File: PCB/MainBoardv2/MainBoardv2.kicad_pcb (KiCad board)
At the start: 2 copper layers, 100 x 100 mm, 100 parts, among them J1 Conn_02x03_Odd_Even, J10 Conn_01x04_Socket, J11 Conn_01x03_Socket, J12 Conn_01x03_Socket, J13 Conn_01x04_Socket, J14 Conn_01x03_Socket, J15 Conn_01x03_Socket, J16 Conn_01x04_Socket, J17 Conn_01x03_Socket, J18 Conn_01x03_Socket, J19 Conn_01x04_Socket, J2 USB_B_Micro, J20 Conn_01x03_Socket, J21 Screw_Terminal_01x02, J22 Screw_Terminal_01x02, J23 Screw_Terminal_01x02, J3 Conn_02x03_Odd_Even, J4 Conn_01x05_Pin, J5 Conn_01x03_Socket, J6 Screw_Terminal_01x02, J7 Conn_01x04_Socket, J8 Screw_Terminal_01x02, J9 Conn_01x04_Socket, SW1 SW_Push, SW2 Toggle, SW3 Slide, U1 AZ1117-3.3, U2 STM32F103C8T6TR, U3 SN74HCS4075PWR, U4 TPS56637RPA, Y1 8MHz Crystal

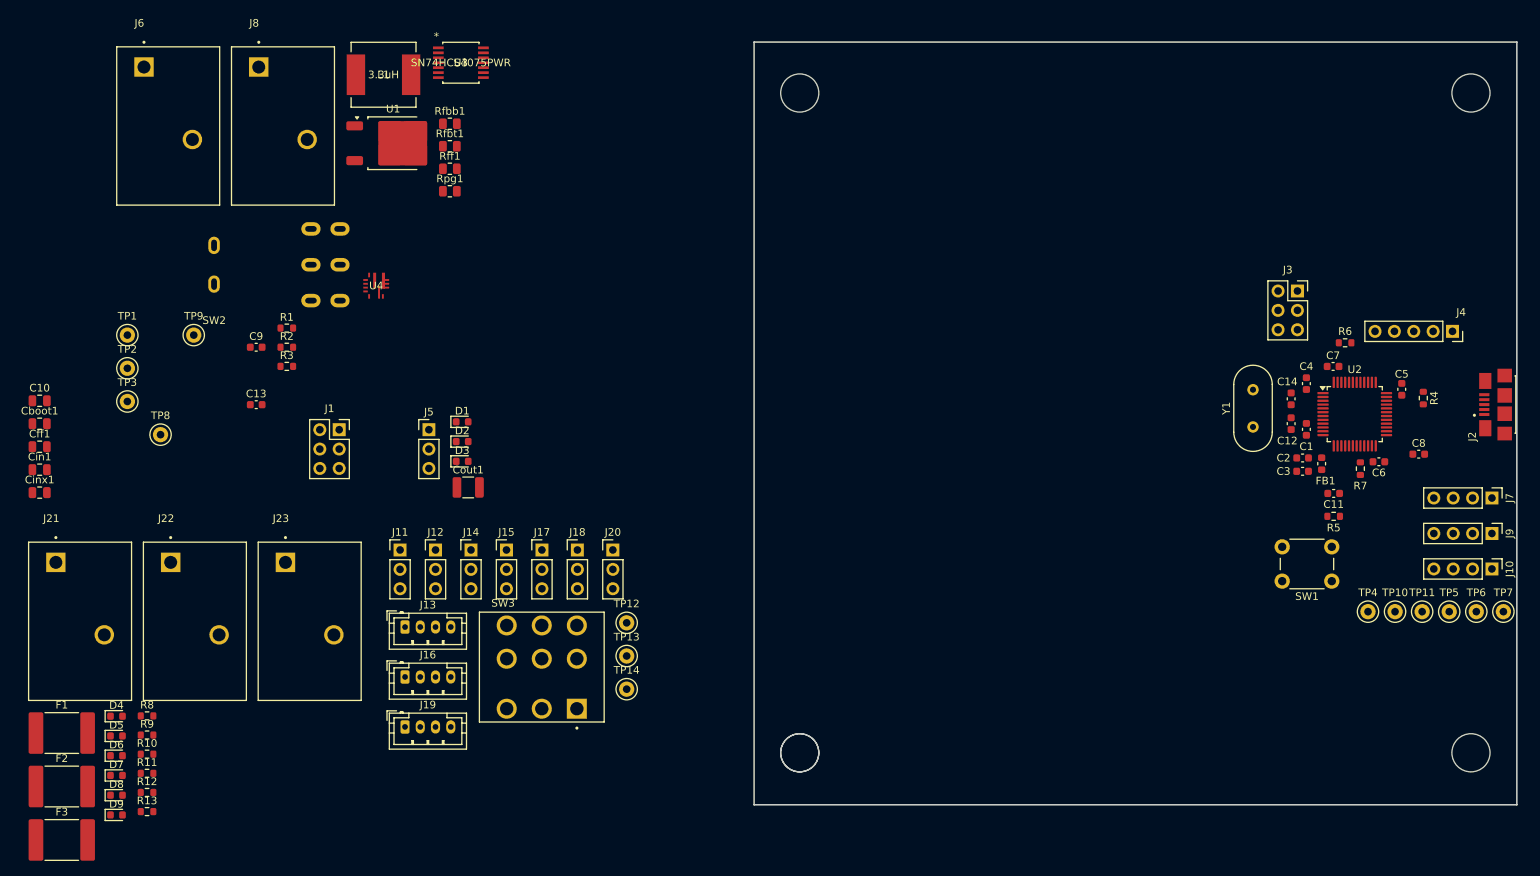
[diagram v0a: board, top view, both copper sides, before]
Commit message: Main Board v2 Rough component layout complete
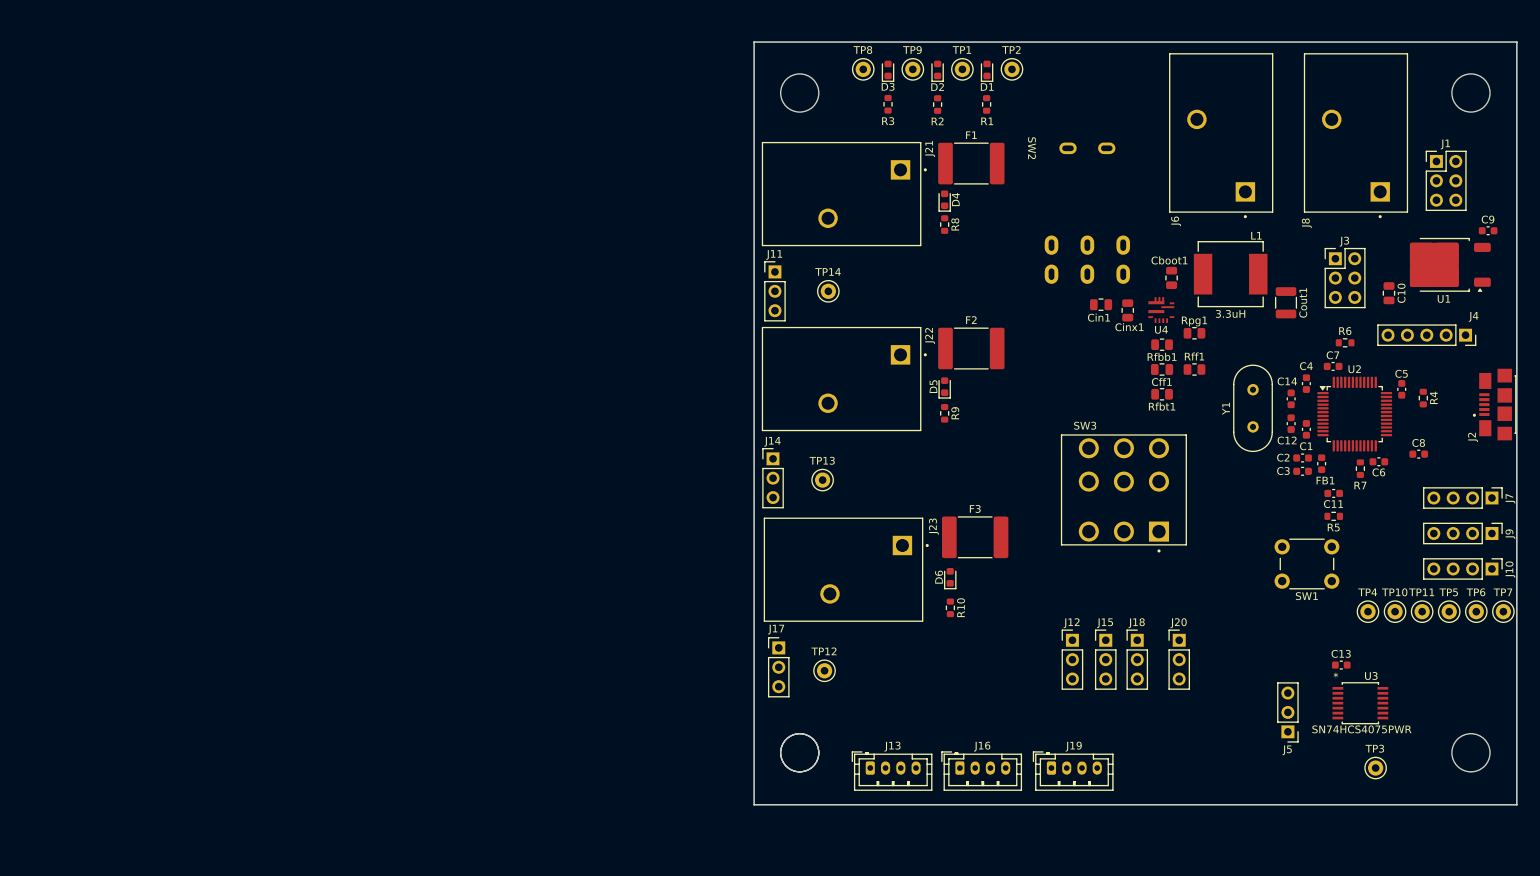
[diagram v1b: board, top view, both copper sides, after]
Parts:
- removed the D5 at (7.17, 137.5)
- removed D7, D8, D9: LED, LED_SMD:LED_0603_1608Metric
- removed R11, R13: 1.5k, Resistor_SMD:R_0603_1608Metric
- removed the R9 at (11.2, 137.4)
- added D6: LED, LED_SMD:LED_0603_1608Metric, F.Cu at (116.5, 116.8)
- J1, J3: footprint Connector_PinSocket_2.54mm:PinSocket_2x03_P2.54mm_Vertical -> Connector_PinHeader_2.54mm:PinHeader_2x03_P2.54mm_Vertical
- moved C10 177.5 mm to (174.0, 79.5), turned to -90 degrees
- moved TP3 170.6 mm to (172.2, 141.8)
- moved C9 162.2 mm to (187.0, 71.3)
- moved J8 155.4 mm to (176.4, 48.1), turned to 180 degrees
- moved J6 152.8 mm to (158.8, 48.1), turned to 180 degrees
- moved Cboot1 149.6 mm to (145.5, 77.5), turned to 90 degrees
- moved J1 148.1 mm to (180.2, 62.2)
- moved Cff1 147.5 mm to (144.2, 89.5), turned to 180 degrees
- moved C13 146.3 mm to (167.8, 128.2)
- moved U3 144.8 mm to (170.2, 133.2)
- moved Cinx1 144.6 mm to (139.8, 81.8), turned to -90 degrees
- moved Cin1 140.8 mm to (136.2, 81.0), turned to 180 degrees
- moved F1 140.7 mm to (119.2, 62.5)
- moved U1 138.7 mm to (181.2, 75.8), turned to 180 degrees
- moved F2 132.4 mm to (119.2, 86.8)
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- renumbered D6 to D5, R12 to R10, R10 to R9
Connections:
- net /PWM & Encoders/M1_PWM renamed /PWM & Encoders & Limit Switches/M1_PWM
- net /PWM & Encoders/M2_PWM renamed /PWM & Encoders & Limit Switches/M2_PWM
- net /PWM & Encoders/M3_PWM renamed /PWM & Encoders & Limit Switches/M3_PWM
- net /PWM & Encoders/RC_PWM1 renamed /PWM & Encoders & Limit Switches/RC_PWM1
- net /PWM & Encoders/RC_PWM2 renamed /PWM & Encoders & Limit Switches/RC_PWM2
- net /PWM & Encoders/RC_PWM3 renamed /PWM & Encoders & Limit Switches/RC_PWM3
- net Net-(D4-A) renamed /Motors/Motor1PowerOut
- net Net-(D6-A) renamed /Motors/Motor2PowerOut
- net Net-(D8-A) renamed /Motors/Motor3PowerOut
- net Net-(J6-Pin_2) renamed /12VPowerInput
- J1 pad 1: VBUS -> /5V_EXT
- J1 pad 5: /5V_EXT -> VBUS
- J11 pad 2: /PWM & Encoders/REG_IN -> +5V
- J14 pad 2: /PWM & Encoders/REG_IN -> +5V
- J17 pad 2: /PWM & Encoders/REG_IN -> +5V
- J20 pad 2: /PWM & Encoders/REG_IN -> +5V
- SW2 pad 3: unconnected-(SW2-C-Pad3) -> /PowerSwitchOff
- SW2 pad 6: unconnected-(SW2-C-Pad6) -> /PowerSwitchOff

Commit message: updating layout progress, adding limit switch extra circuitry
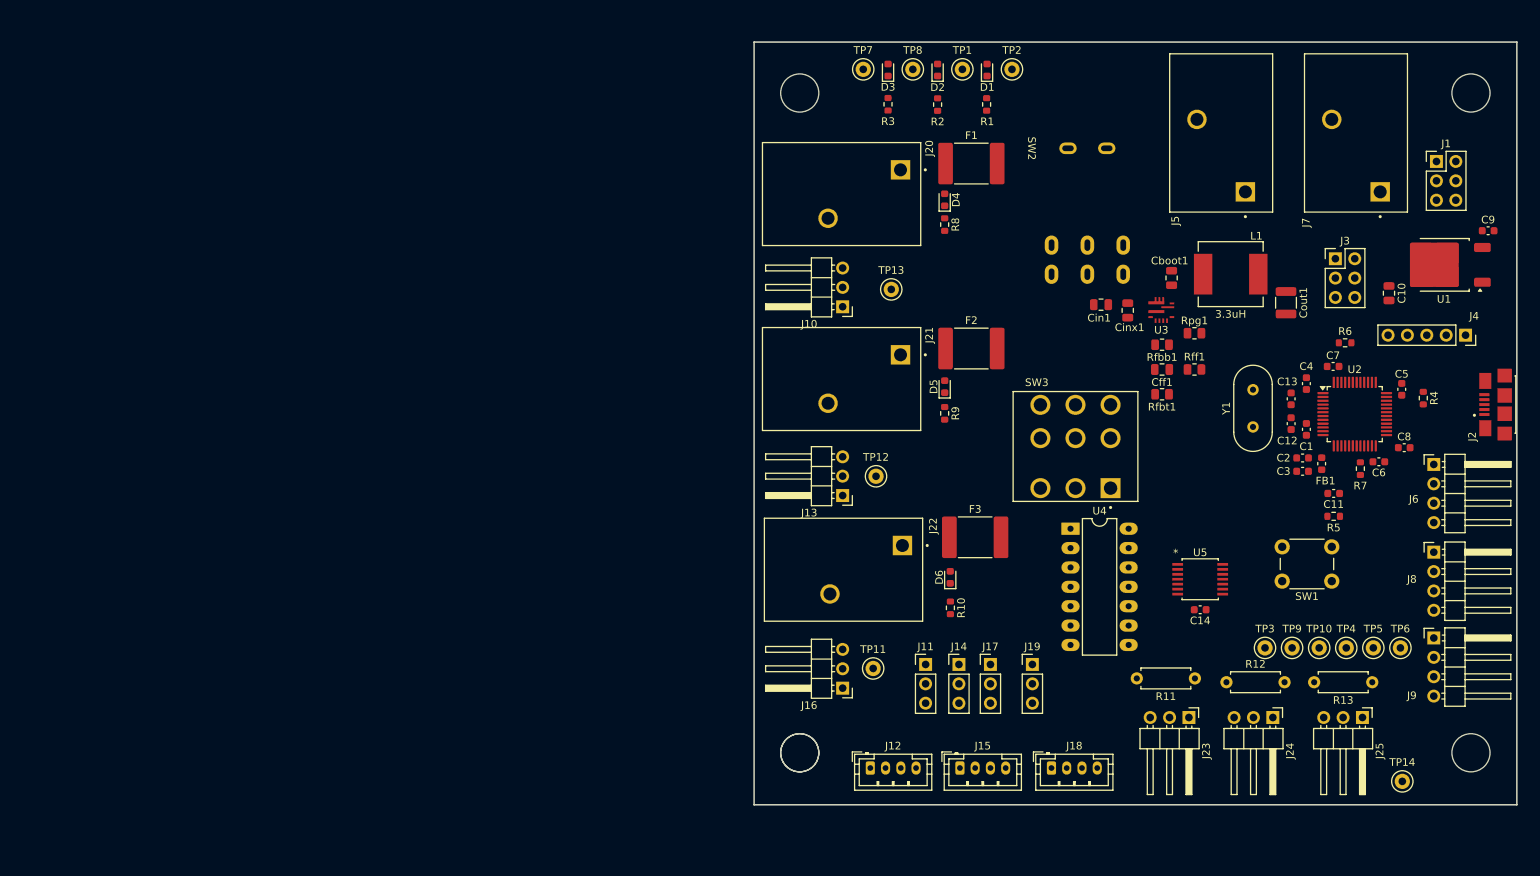
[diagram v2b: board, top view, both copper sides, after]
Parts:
- removed the C13 at (167.8, 128.2)
- removed the J5 at (160.8, 137.0)
- removed the TP3 at (172.2, 141.8)
- removed the U3 at (170.2, 133.2)
- added C14: 100n, Capacitor_SMD:C_0603_1608Metric, F.Cu at (149.2, 121.0)
- added J23: Conn_01x03_Socket, Connector_PinHeader_2.54mm:PinHeader_1x03_P2.54mm_Horizontal, F.Cu at (147.8, 135.1)
- added J24: Conn_01x03_Socket, Connector_PinHeader_2.54mm:PinHeader_1x03_P2.54mm_Horizontal, F.Cu at (158.8, 135.1)
- added J25: Conn_01x03_Socket, Connector_PinHeader_2.54mm:PinHeader_1x03_P2.54mm_Horizontal, F.Cu at (170.5, 135.1)
- added R11: 10k, Resistor_THT:R_Axial_DIN0207_L6.3mm_D2.5mm_P7.62mm_Horizontal, F.Cu at (148.6, 130.0)
- added R12: 10k, Resistor_THT:R_Axial_DIN0207_L6.3mm_D2.5mm_P7.62mm_Horizontal, F.Cu at (152.7, 130.5)
- added R13: 10k, Resistor_THT:R_Axial_DIN0207_L6.3mm_D2.5mm_P7.62mm_Horizontal, F.Cu at (171.8, 130.5)
- added TP14: White, TestPoint:TestPoint_Keystone_5000-5004_Miniature, F.Cu at (175.8, 143.5)
- added U4: CD74HC00_N_14, Package_DIP:DIP-14_W7.62mm_LongPads, F.Cu at (132.2, 110.4)
- added U5: SN74HCS4075PWR, CustomFootprints:SN74HCS4075PWR, F.Cu at (149.2, 117.0)
- J10: renamed from J11; footprint Connector_PinHeader_2.54mm:PinHeader_1x03_P2.54mm_Vertical -> Connector_PinHeader_2.54mm:PinHeader_1x03_P2.54mm_Horizontal
- J13: renamed from J14; footprint Connector_PinHeader_2.54mm:PinHeader_1x03_P2.54mm_Vertical -> Connector_PinHeader_2.54mm:PinHeader_1x03_P2.54mm_Horizontal
- J16: renamed from J17; footprint Connector_PinHeader_2.54mm:PinHeader_1x03_P2.54mm_Vertical -> Connector_PinHeader_2.54mm:PinHeader_1x03_P2.54mm_Horizontal
- J6: renamed from J7; footprint Connector_PinHeader_2.54mm:PinHeader_1x04_P2.54mm_Vertical -> Connector_PinHeader_2.54mm:PinHeader_1x04_P2.54mm_Horizontal
- J8: renamed from J9; footprint Connector_PinHeader_2.54mm:PinHeader_1x04_P2.54mm_Vertical -> Connector_PinHeader_2.54mm:PinHeader_1x04_P2.54mm_Horizontal
- J9: renamed from J10; footprint Connector_PinHeader_2.54mm:PinHeader_1x04_P2.54mm_Vertical -> Connector_PinHeader_2.54mm:PinHeader_1x04_P2.54mm_Horizontal
- moved J11 19.5 mm to (113.2, 128.2)
- moved J14 19.5 mm to (117.6, 128.2)
- moved J17 19.5 mm to (121.8, 128.2)
- moved J19 19.5 mm to (127.2, 128.2)
- moved TP10 14.3 mm to (164.8, 126.0)
- moved TP3 14.3 mm to (157.8, 126.0)
- moved TP4 14.3 mm to (168.4, 126.0)
- moved TP5 14.3 mm to (171.9, 126.0)
- moved TP6 14.3 mm to (175.5, 126.0)
- moved TP9 14.3 mm to (161.3, 126.0)
- moved J9 11.8 mm to (179.9, 124.7), turned to 0 degrees
- moved J13 10.3 mm to (102.4, 106.0), turned to 180 degrees
- moved J10 9.98 mm to (102.4, 81.3), turned to 180 degrees
- moved J16 9.90 mm to (102.4, 131.3), turned to 180 degrees
- moved J6 8.80 mm to (179.9, 102.0), turned to 0 degrees
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- renumbered C14 to C13, J12 to J11, J13 to J12, J15 to J14, J16 to J15, J18 to J17, J19 to J18, J20 to J19, J21 to J20, J22 to J21, J23 to J22, J6 to J5, J8 to J7, TP11 to TP10, TP12 to TP11, TP13 to TP12, TP14 to TP13, TP4 to TP3, TP5 to TP4, TP6 to TP5, TP7 to TP6, TP8 to TP7, TP9 to TP8, TP10 to TP9, U4 to U3

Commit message: PCB laid out & passes DRC
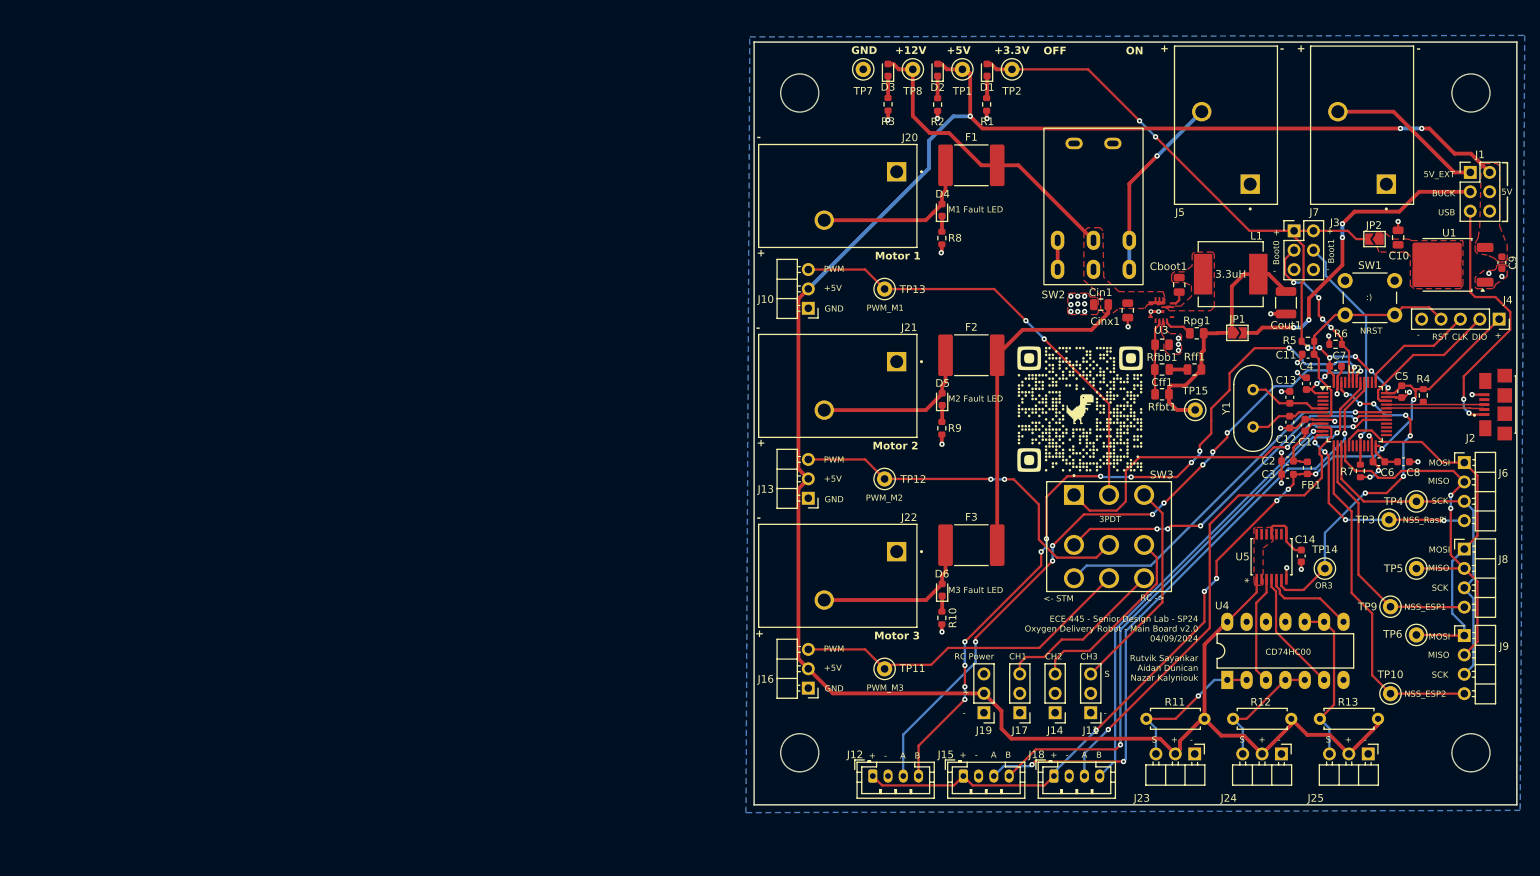
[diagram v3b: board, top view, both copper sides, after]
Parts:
- removed ?: , 
- added G***: LOGO, LOGO, F.Cu at (133.5, 94.7)
- added JP1: SolderJumper_2_Open, Jumper:SolderJumper-2_P1.3mm_Open_TrianglePad1.0x1.5mm, F.Cu at (154.1, 84.7)
- added JP2: SolderJumper_2_Open, Jumper:SolderJumper-2_P1.3mm_Open_TrianglePad1.0x1.5mm, F.Cu at (172.1, 72.4)
- added TP15: 5V_Buck, TestPoint:TestPoint_Keystone_5000-5004_Miniature, F.Cu at (148.6, 94.8)
- moved SW1 39.4 mm to (168.2, 77.8), turned to 0 degrees
- moved TP14 29.7 mm to (165.6, 115.6)
- moved U4 28.6 mm to (152.8, 130.2), turned to 90 degrees
- moved TP3 23.4 mm to (174.0, 109.2)
- moved R5 23.2 mm to (163.4, 85.8)
- moved J11 22.6 mm to (134.9, 134.5), turned to 180 degrees
- moved TP4 21.3 mm to (177.6, 106.8)
- moved C11 18.6 mm to (163.4, 87.5)
- moved C14 15.0 mm to (162.5, 113.9), turned to -90 degrees
- moved J14 14.1 mm to (130.2, 134.5), turned to 180 degrees
- moved TP9 14.0 mm to (174.2, 120.6)
- moved SW3 12.6 mm to (137.3, 111.4), turned to 180 degrees
- moved TP5 11.8 mm to (177.6, 115.6)
- moved TP10 11.1 mm to (174.2, 132.0)
- moved U5 9.81 mm to (158.6, 114.0), turned to 90 degrees
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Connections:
- C10 pad 1: +3.3V -> /REG_OUT
- Cout1 pad 1: /5V_BUCK -> /5V_BUCK_JumperIN
- L1 pad 2: /5V_BUCK -> /5V_BUCK_JumperIN
- Rfbt1 pad 2: /5V_BUCK -> /5V_BUCK_JumperIN
- Rff1 pad 2: /5V_BUCK -> /5V_BUCK_JumperIN
- Rpg1 pad 2: /5V_BUCK -> /5V_BUCK_JumperIN
- U1 pad 2: +3.3V -> /REG_OUT
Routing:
- net +5V: track 0.00 -> 286.3 mm, vias 0 -> 3
- net +3.3V: track 0.00 -> 224.9 mm, vias 0 -> 18
- net /TIM4_CH2: track 0.00 -> 99.5 mm, vias 0 -> 12
- net /TIM4_CH1: track 0.00 -> 90.7 mm, vias 0 -> 9
- net +12V: track 0.00 -> 83.0 mm
- net /TIM3_CH1: track 0.00 -> 82.7 mm, vias 0 -> 3
- net /TIM3_CH2: track 0.00 -> 78.5 mm, vias 0 -> 2
- net /TIM2_CH1: track 0.00 -> 65.3 mm, vias 0 -> 1
- net /PWM & Encoders & Limit Switches/M1_PWM: track 0.00 -> 58.7 mm, vias 0 -> 2
- net /TIM2_CH2: track 0.00 -> 58.1 mm, vias 0 -> 1
- net /SPI1_MISO: track 0.00 -> 51.3 mm, vias 0 -> 2
- net /TIM1_CH3: track 0.00 -> 50.0 mm, vias 0 -> 1
- net /SPI1_MOSI: track 0.00 -> 49.9 mm
- net /TIM1_CH1: track 0.00 -> 49.4 mm, vias 0 -> 2
- net GND: track 0.00 -> 49.4 mm, vias 0 -> 42
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- added copper zone on F.Cu, net +12V
- added copper zone on F.Cu, net +5V
- added copper zone on F.Cu, net /REG_OUT
- added copper zone on F.Cu, net /SW
- added copper zone on B.Cu, net GND
- added copper zone on F.Cu, net GND
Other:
- board text added: "+"
- board text added: "+12V"
- board text added: "+3.3V"
- board text added: "+5V"
- board text added: "-"
- board text added: "3PDT"
- board text added: "5V"
- board text added: "5V_EXT"
- board text added: ":)"
- board text added: "<- STM"
- board text added: "A"
- board text added: "B"
- board text added: "BUCK"
- board text added: "Boot0"
- board text added: "Boot1"
- board text added: "CD74HC00"
- board text added: "CH1"
- board text added: "CH2"
- board text added: "CH3"
- board text added: "CLK"
- board text added: "DIO"
- board text added: "ECE 445 - Senior Design Lab - SP24 Oxygen Delivery Robot - Main Board v2.0 04/09/2024 Rutvik Sayankar Aidan Dunican Nazar Kalyniouk"
- board text added: "GND"
- board text added: "M1 Fault LED"
- board text added: "M2 Fault LED"
- board text added: "M3 Fault LED"
- board text added: "MISO"
- board text added: "MOSI"
- board text added: "Motor 1"
- board text added: "Motor 2"
- board text added: "Motor 3"
- board text added: "NRST"
- board text added: "NSS_ESP1"
- board text added: "NSS_ESP2"
- board text added: "NSS_RasPi"
- board text added: "OFF"
- board text added: "ON"
- board text added: "OR3"
- board text added: "PWM"
- board text added: "PWM_M1"
- board text added: "PWM_M2"
- board text added: "PWM_M3"
- board text added: "RC ->"
- board text added: "RC Power"
- board text added: "RST"
- board text added: "S"
- board text added: "SCK"
- board text added: "USB"
